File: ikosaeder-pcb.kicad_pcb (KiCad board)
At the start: 2 copper layers, 21.9 x 20.8 mm, 0 parts

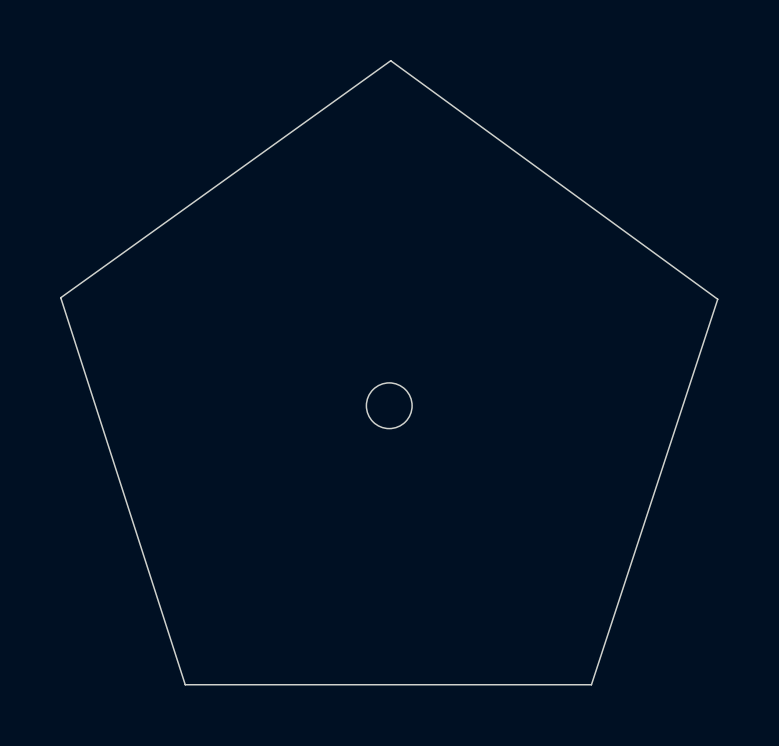
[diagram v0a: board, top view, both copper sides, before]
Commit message: Add GND/ 5V and standard headers
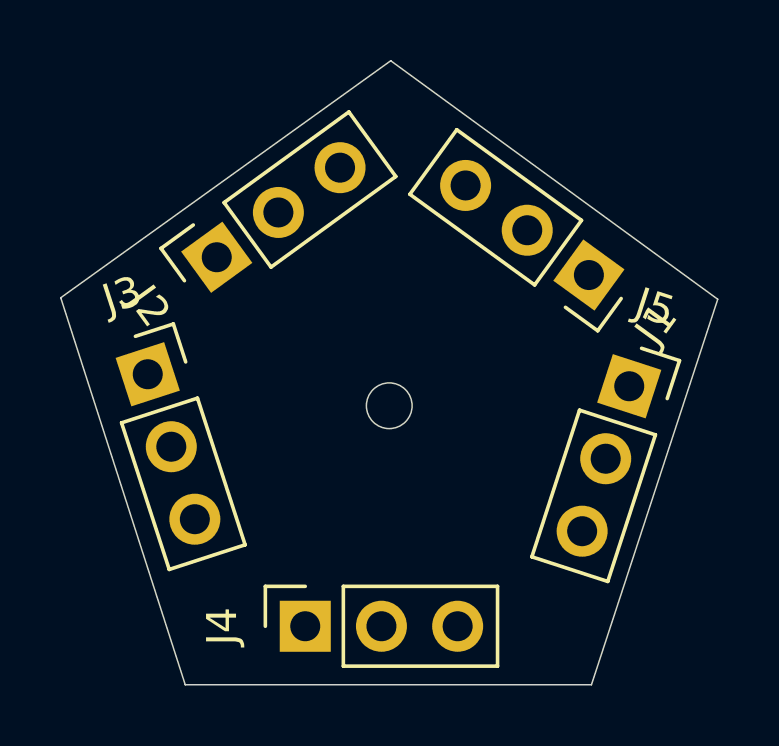
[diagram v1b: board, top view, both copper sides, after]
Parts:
- added J1: Conn_01x03_Female, Connector_PinSocket_2.54mm:PinSocket_1x03_P2.54mm_Vertical, F.Cu at (113.5, 86.3)
- added J2: Conn_01x03_Female, Connector_PinSocket_2.54mm:PinSocket_1x03_P2.54mm_Vertical, F.Cu at (101.0, 85.8)
- added J3: Conn_01x03_Female, Connector_PinSocket_2.54mm:PinSocket_1x03_P2.54mm_Vertical, F.Cu at (98.8, 89.7)
- added J4: Conn_01x03_Female, Connector_PinSocket_2.54mm:PinSocket_1x03_P2.54mm_Vertical, F.Cu at (104.0, 98.0)
- added J5: Conn_01x03_Female, Connector_PinSocket_2.54mm:PinSocket_1x03_P2.54mm_Vertical, F.Cu at (114.8, 90.0)

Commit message: Make the first pcb board which has the label A
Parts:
- removed J1, J2, J3, J4, J5: Conn_01x03_Female, Connector_PinSocket_2.54mm:PinSocket_1x03_P2.54mm_Vertical
- added <C-34: Conn_01x03_Female, Connector_PinSocket_2.54mm:PinSocket_1x03_P2.54mm_Vertical, F.Cu at (109.0, 93.7)
- added <D-30: Conn_01x03_Female, Connector_PinSocket_2.54mm:PinSocket_1x03_P2.54mm_Vertical, F.Cu at (114.0, 86.6)
- added >B-35: Conn_01x03_Female, Connector_PinSocket_2.54mm:PinSocket_1x03_P2.54mm_Vertical, F.Cu at (99.4, 86.4)
- added >E-1: Conn_01x03_Female, Connector_PinSocket_2.54mm:PinSocket_1x03_P2.54mm_Vertical, F.Cu at (112.8, 82.7)
- added >F-31: Conn_01x03_Female, Connector_PinSocket_2.54mm:PinSocket_1x03_P2.54mm_Vertical, F.Cu at (104.9, 79.9)
- added Power1: Conn_01x02_Female, Connector_PinHeader_2.54mm:PinHeader_1x02_P2.54mm_Vertical, B.Cu at (103.8, 85.3)
- added Signal1: Conn_01x01_Female, Connector_PinHeader_2.54mm:PinHeader_1x01_P2.54mm_Vertical, B.Cu at (109.7, 85.3)
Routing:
- net Net-(<D-30-Pad2): track 0.00 -> 13.5 mm
- net Net-(<C-34-Pad2): track 0.00 -> 8.21 mm
- net Net-(>E-1-Pad2): track 0.00 -> 4.60 mm
- added copper zone on B.Cu, net +5V
- added copper zone on F.Cu, net GND
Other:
- outline, holes or cut-outs redrawn
- board text added: "5V"
- board text added: "A"
- board text added: "GND"

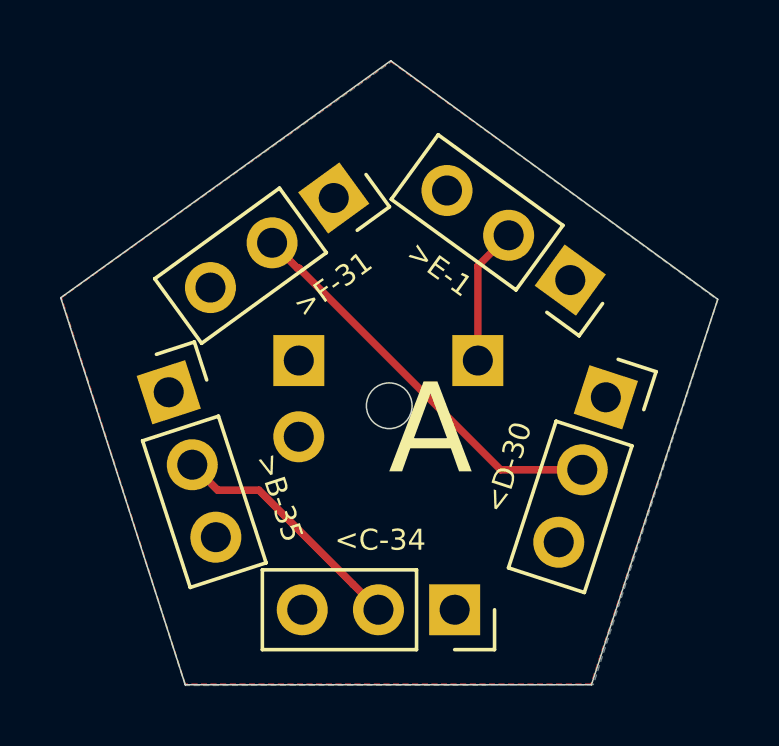
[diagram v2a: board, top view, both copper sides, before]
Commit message: Minor tweaks
- Add male / female connector for semantic purposes
- Consolidate the connectors
- Prepare for 12 pcbs
- Use clockwise arrangement
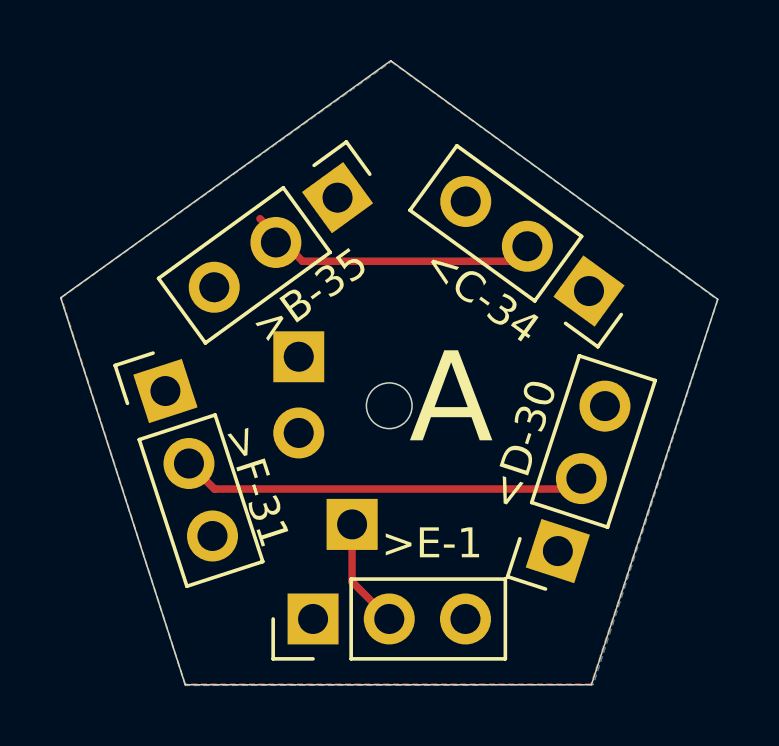
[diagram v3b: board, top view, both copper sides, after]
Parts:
- removed Signal1: Conn_01x01_Female, Connector_PinHeader_2.54mm:PinHeader_1x01_P2.54mm_Vertical
- added DIN1: Conn_01x01_Female, Connector_PinHeader_2.54mm:PinHeader_1x01_P2.54mm_Vertical, B.Cu at (105.5, 90.8)
- >B-35, >E-1, >F-31: value Conn_01x03_Female -> Conn_01x03_Male; footprint Connector_PinSocket_2.54mm:PinSocket_1x03_P2.54mm_Vertical -> Connector_PinHeader_2.54mm:PinHeader_1x03_P2.54mm_Vertical
- moved >E-1 14.2 mm to (104.2, 94.0), turned to 90 degrees
- moved <C-34 11.5 mm to (113.4, 83.0), turned to 234 degrees
- moved >B-35 8.59 mm to (105.1, 79.9), turned to 306 degrees
- moved >F-31 8.54 mm to (99.3, 86.4), turned to 18 degrees
- moved <D-30 5.37 mm to (112.4, 91.7), turned to 162 degrees
- moved Power1 0.13 mm to (103.8, 85.2)
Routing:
- net Net-(<C-34-Pad2): track 8.21 -> 10.2 mm
- net Net-(>E-1-Pad2): track 4.60 -> 3.67 mm
- added copper zone on F.Cu, net +5V
- added copper zone on B.Cu, net GND
- removed copper zone on B.Cu, net +5V
- removed copper zone on F.Cu, net GND
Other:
- board text added: "DIN"

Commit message: Ikosaeder final
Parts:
- removed <C-34, <D-30: Conn_01x03_Female, Connector_PinSocket_2.54mm:PinSocket_1x03_P2.54mm_Vertical
- removed >B-35, >E-1, >F-31: Conn_01x03_Male, Connector_PinHeader_2.54mm:PinHeader_1x03_P2.54mm_Vertical
- added <=C.21: Conn_01x01_Female, Connector_PinHeader_2.54mm:PinHeader_1x01_P2.54mm_Vertical, F.Cu at (174.1, 105.6)
- added <=D.13: Conn_01x01_Female, Connector_PinHeader_2.54mm:PinHeader_1x01_P2.54mm_Vertical, F.Cu at (108.8, 127.4)
- added <=E.15: Conn_01x01_Female, Connector_PinHeader_2.54mm:PinHeader_1x01_P2.54mm_Vertical, F.Cu at (129.5, 132.4)
- added <=F.25: Conn_01x01_Female, Connector_PinHeader_2.54mm:PinHeader_1x01_P2.54mm_Vertical, F.Cu at (151.4, 128.3)
- added <=G.9: Conn_01x01_Female, Connector_PinHeader_2.54mm:PinHeader_1x01_P2.54mm_Vertical, F.Cu at (173.9, 127.4)
- added <A.1: LEDs_In, IkosaederFootprints:LED-Strip, F.Cu at (106.4, 114.8)
- added <A.31: LEDs_In, IkosaederFootprints:LED-Strip, F.Cu at (125.6, 102.6)
- added <A.35: LEDs_In, IkosaederFootprints:LED-Strip, F.Cu at (125.5, 81.3)
- added <B.27: LEDs_In, IkosaederFootprints:LED-Strip, F.Cu at (148.8, 102.6)
- added <B.33: LEDs_In, IkosaederFootprints:LED-Strip, F.Cu at (148.5, 81.1)
- added <C.29: LEDs_In, IkosaederFootprints:LED-Strip, F.Cu at (171.7, 81.2)
- added <C.34: LEDs_In, IkosaederFootprints:LED-Strip, F.Cu at (103.0, 81.2)
- added <D.23: LEDs_In, IkosaederFootprints:LED-Strip, F.Cu at (113.0, 110.4)
- added <D.30: LEDs_In, IkosaederFootprints:LED-Strip, F.Cu at (100.3, 88.8)
- added <E.2: LEDs_In, IkosaederFootprints:LED-Strip, F.Cu at (129.5, 136.9)
- added <E.24: LEDs_In, IkosaederFootprints:LED-Strip, F.Cu at (123.1, 110.4)
- added <F.17: LEDs_In, IkosaederFootprints:LED-Strip, F.Cu at (148.3, 124.5)
- added <F.32: LEDs_In, IkosaederFootprints:LED-Strip, F.Cu at (122.9, 88.9)
- added <G.19: LEDs_In, IkosaederFootprints:LED-Strip, F.Cu at (169.1, 110.1)
- added <G.28: LEDs_In, IkosaederFootprints:LED-Strip, F.Cu at (145.9, 89.0)
- added <H.11: LEDs_In, IkosaederFootprints:LED-Strip, F.Cu at (102.5, 124.5)
- added <H.20: LEDs_In, IkosaederFootprints:LED-Strip, F.Cu at (152.6, 93.7)
- added <H.22: LEDs_In, IkosaederFootprints:LED-Strip, F.Cu at (168.7, 89.0)
- added <I.12: LEDs_In, IkosaederFootprints:LED-Strip, F.Cu at (175.4, 93.6)
- added <I.14: LEDs_In, IkosaederFootprints:LED-Strip, F.Cu at (111.0, 102.9)
- added <I.7: LEDs_In, IkosaederFootprints:LED-Strip, F.Cu at (181.7, 132.2)
- added <J.16: LEDs_In, IkosaederFootprints:LED-Strip, F.Cu at (129.5, 115.1)
- added <J.3: LEDs_In, IkosaederFootprints:LED-Strip, F.Cu at (175.3, 136.9)
- added <J.6: LEDs_In, IkosaederFootprints:LED-Strip, F.Cu at (106.7, 136.9)
- added <K.18: LEDs_In, IkosaederFootprints:LED-Strip, F.Cu at (146.5, 110.4)
- added <K.26: LEDs_In, IkosaederFootprints:LED-Strip, F.Cu at (129.5, 93.9)
- added <K.5: LEDs_In, IkosaederFootprints:LED-Strip, F.Cu at (135.9, 132.2)
- added <L.10: LEDs_In, IkosaederFootprints:LED-Strip, F.Cu at (175.6, 114.9)
- added <L.4: LEDs_In, IkosaederFootprints:LED-Strip, F.Cu at (152.4, 136.8)
- added <L.8: LEDs_In, IkosaederFootprints:LED-Strip, F.Cu at (152.9, 114.9)
- added =>H.21: Conn_01x01_Male, Connector_PinHeader_2.54mm:PinHeader_1x01_P2.54mm_Vertical, F.Cu at (152.6, 89.2)
- added =>I.13: Conn_01x01_Male, Connector_PinHeader_2.54mm:PinHeader_1x01_P2.54mm_Vertical, F.Cu at (175.7, 89.9)
- added =>J.15: Conn_01x01_Male, Connector_PinHeader_2.54mm:PinHeader_1x01_P2.54mm_Vertical, F.Cu at (105.2, 106.4)
- added =>K.25: Conn_01x01_Male, Connector_PinHeader_2.54mm:PinHeader_1x01_P2.54mm_Vertical, F.Cu at (132.3, 109.2)
- added =>L.9: Conn_01x01_Male, Connector_PinHeader_2.54mm:PinHeader_1x01_P2.54mm_Vertical, F.Cu at (153.2, 111.3)
- added >A.30: LEDs_Out, IkosaederFootprints:LED-Strip, F.Cu at (179.7, 81.4)
- added >A.34: LEDs_Out, IkosaederFootprints:LED-Strip, F.Cu at (156.7, 81.6)
- added >B.26: LEDs_Out, IkosaederFootprints:LED-Strip, F.Cu at (158.8, 132.1)
- added >B.32: LEDs_Out, IkosaederFootprints:LED-Strip, F.Cu at (133.6, 102.6)
- added >B.35: LEDs_Out, IkosaederFootprints:LED-Strip, F.Cu at (110.6, 81.4)
- added >C.20: LEDs_Out, IkosaederFootprints:LED-Strip, F.Cu at (171.8, 102.6)
- added >C.28: LEDs_Out, IkosaederFootprints:LED-Strip, F.Cu at (157.1, 102.7)
- added >C.33: LEDs_Out, IkosaederFootprints:LED-Strip, F.Cu at (134.0, 81.4)
- added >D.12: LEDs_Out, IkosaederFootprints:LED-Strip, F.Cu at (110.9, 124.6)
- added >D.22: LEDs_Out, IkosaederFootprints:LED-Strip, F.Cu at (180.1, 102.8)
- added >D.29: LEDs_Out, IkosaederFootprints:LED-Strip, F.Cu at (159.1, 88.9)
- added >E.1: LEDs_Out, IkosaederFootprints:LED-Strip, F.Cu at (106.9, 93.5)
- added >E.14: LEDs_Out, IkosaederFootprints:LED-Strip, F.Cu at (113.3, 132.2)
- added >E.23: LEDs_Out, IkosaederFootprints:LED-Strip, F.Cu at (181.9, 88.9)
- added >F.16: LEDs_Out, IkosaederFootprints:LED-Strip, F.Cu at (133.3, 124.5)
- added >F.24: LEDs_Out, IkosaederFootprints:LED-Strip, F.Cu at (100.3, 110.2)
- added >F.31: LEDs_Out, IkosaederFootprints:LED-Strip, F.Cu at (113.3, 88.8)
- added >G.18: LEDs_Out, IkosaederFootprints:LED-Strip, F.Cu at (156.7, 124.6)
- added >G.27: LEDs_Out, IkosaederFootprints:LED-Strip, F.Cu at (136.1, 89.2)
- added >G.8: LEDs_Out, IkosaederFootprints:LED-Strip, F.Cu at (171.3, 124.3)
- added >H.10: LEDs_Out, IkosaederFootprints:LED-Strip, F.Cu at (179.5, 124.6)
- added >H.19: LEDs_Out, IkosaederFootprints:LED-Strip, F.Cu at (159.5, 110.2)
- added >I.11: LEDs_Out, IkosaederFootprints:LED-Strip, F.Cu at (182.2, 110.4)
- added >I.6: LEDs_Out, IkosaederFootprints:LED-Strip, F.Cu at (125.5, 124.7)
- added >J.2: LEDs_Out, IkosaederFootprints:LED-Strip, F.Cu at (102.6, 102.6)
- added >J.5: LEDs_Out, IkosaederFootprints:LED-Strip, F.Cu at (146.1, 132.1)
- added >K.17: LEDs_Out, IkosaederFootprints:LED-Strip, F.Cu at (136.0, 110.2)
- added >K.4: LEDs_Out, IkosaederFootprints:LED-Strip, F.Cu at (168.8, 132.2)
- added >L.3: LEDs_Out, IkosaederFootprints:LED-Strip, F.Cu at (123.1, 132.2)
- added >L.7: LEDs_Out, IkosaederFootprints:LED-Strip, F.Cu at (100.3, 132.2)
- added G***: LOGO, LOGO, B.Cu at (175.3, 123.9)
- added G***: LOGO, LOGO, B.Cu at (152.4, 87.1)
- added G***: LOGO, LOGO, B.Cu at (132.8, 91.9)
- added G***: LOGO, LOGO, B.Cu at (152.5, 130.2)
- added G***: LOGO, LOGO, B.Cu at (135.4, 128.2)
- added G***: LOGO, LOGO, B.Cu at (106.7, 124.0)
- added G***: LOGO, LOGO, B.Cu at (110.3, 113.4)
- added G***: LOGO, LOGO, B.Cu at (125.8, 113.8)
- added G***: LOGO, LOGO, B.Cu at (153.1, 102.0)
- added G***: LOGO, LOGO, B.Cu at (170.0, 106.5)
- added G***: LOGO, LOGO, B.Cu at (179.4, 92.3)
- added JP1: SolderJumper_2_Bridged, Jumper:SolderJumper-2_P1.3mm_Bridged_RoundedPad1.0x1.5mm, F.Cu at (109.2, 105.9)
- moved Power1 2.22 mm to (105.7, 84.1), turned to -90 degrees
- moved DIN1 1.37 mm to (106.8, 90.3)
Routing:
- net +5V: track 0.00 -> 254.8 mm, vias 0 -> 70
- net GND: track 0.00 -> 190.5 mm, vias 0 -> 79
- net Net-(<K.5-Pad2): track 0.00 -> 18.9 mm
- net Net-(<G.28-Pad2): track 0.00 -> 16.5 mm
- net Net-(<I.7-Pad2): track 0.00 -> 16.0 mm
- net Net-(<F.32-Pad2): track 0.00 -> 16.0 mm
- net Net-(<D.30-Pad2): track 0.00 -> 15.9 mm
- net Net-(<H.22-Pad2): track 0.00 -> 14.9 mm
- net Net-(<A.1-Pad2): track 0.00 -> 14.5 mm, vias 0 -> 2
- net Net-(<K.18-Pad2): track 0.00 -> 14.2 mm
- net Net-(<D-30-Pad2): track 13.6 -> 0.00 mm
- net Net-(<D.23-Pad2): track 0.00 -> 13.5 mm
- net Net-(<C.29-Pad2): track 0.00 -> 11.6 mm
- net Net-(<F.17-Pad2): track 0.00 -> 11.5 mm
- net Net-(<A.31-Pad2): track 0.00 -> 11.5 mm
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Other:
- board size 21.9 x 20.8 mm -> 98.9 x 64.3 mm
- net class 5V added: clearance 0.2, trace_width 1, via_dia 0.8, via_drill 0.4
- net class GND added: clearance 0.2, trace_width 1, via_dia 0.8, via_drill 0.4
- board text added: "April 2020"
- board text added: "B"
- board text added: "By BeFaFl"
- board text added: "C"
- board text added: "D"
- board text added: "Designed in Zurich"
- board text added: "E"
- board text added: "EAST"
- board text added: "F"
- board text added: "FIN."
- board text added: "G"
- board text added: "H"
- board text added: "HICKEN!"
- board text added: "I"
- board text added: "J"
- board text added: "JLCJLCJLCJLC"
- board text added: "June-ish 2020"
- board text added: "K"
- board text added: "L"
- board text added: "LE"
- board text added: "Mind the"
- board text added: "NORTH"
- board text added: "NORTHWEST"
- board text added: "Order Nr."
- board text added: "SOUTH"
- board text added: "This is me!"
- board text added: "V1.0"
- board text added: "eep the GND plane"
- board text added: "github.com/BeFaFl"
- board text added: "leen"

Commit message: Fix errors
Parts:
- moved <E.2 12.9 mm to (125.7, 124.6), turned to 36 degrees
- moved >I.6 7.86 mm to (123.2, 132.2), turned to -72 degrees
- moved >L.3 7.86 mm to (129.5, 136.7), turned to 0 degrees
- moved >B.26 7.81 mm to (156.2, 124.7), turned to 144 degrees
- moved >G.18 7.64 mm to (158.8, 132.0), turned to 72 degrees
- moved <=E.15 5.04 mm to (128.0, 127.6), turned to 180 degrees
- moved Power1 4.98 mm to (104.0, 88.8)
- moved DIN1 2.85 mm to (109.2, 88.8)
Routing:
- net +5V: track 254.8 -> 291.4 mm, vias 70 -> 72
- net Net-(<K.5-Pad2): track 18.9 -> 13.5 mm, vias 0 -> 2
- net Net-(<E.2-Pad2): track 9.41 -> 13.6 mm
- net Net-(<F.17-Pad2): track 11.5 -> 15.6 mm
- net Net-(<=F.25-Pad1): track 9.36 -> 6.33 mm
- net GND: track 190.5 -> 192.7 mm, vias 79 -> 77
- net Net-(<=E.15-Pad1): track 9.55 -> 7.51 mm, vias 0 -> 1
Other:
- board text added: "V1.1"
- board text removed: "V1.0"
